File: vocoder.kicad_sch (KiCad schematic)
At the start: 63 parts, among them J1 AudioJack4, J2 Conn_01x02_Socket, J3 Conn_01x02_Pin, J4 USB_C_Receptacle_USB2.0_16P, Q1 Q_NPN_BCE, Q2 Q_NPN_BCE, Q3 AO3401A, Q4 Q_NPN_BCE, SW1 SW_SPDT, SW2 SW_Push, SW3 SW_Push, U1 ESP32-S3-MINI-1, U3 BQ24074RGT, U4 TPS63031DSK, U5 ADAU1761

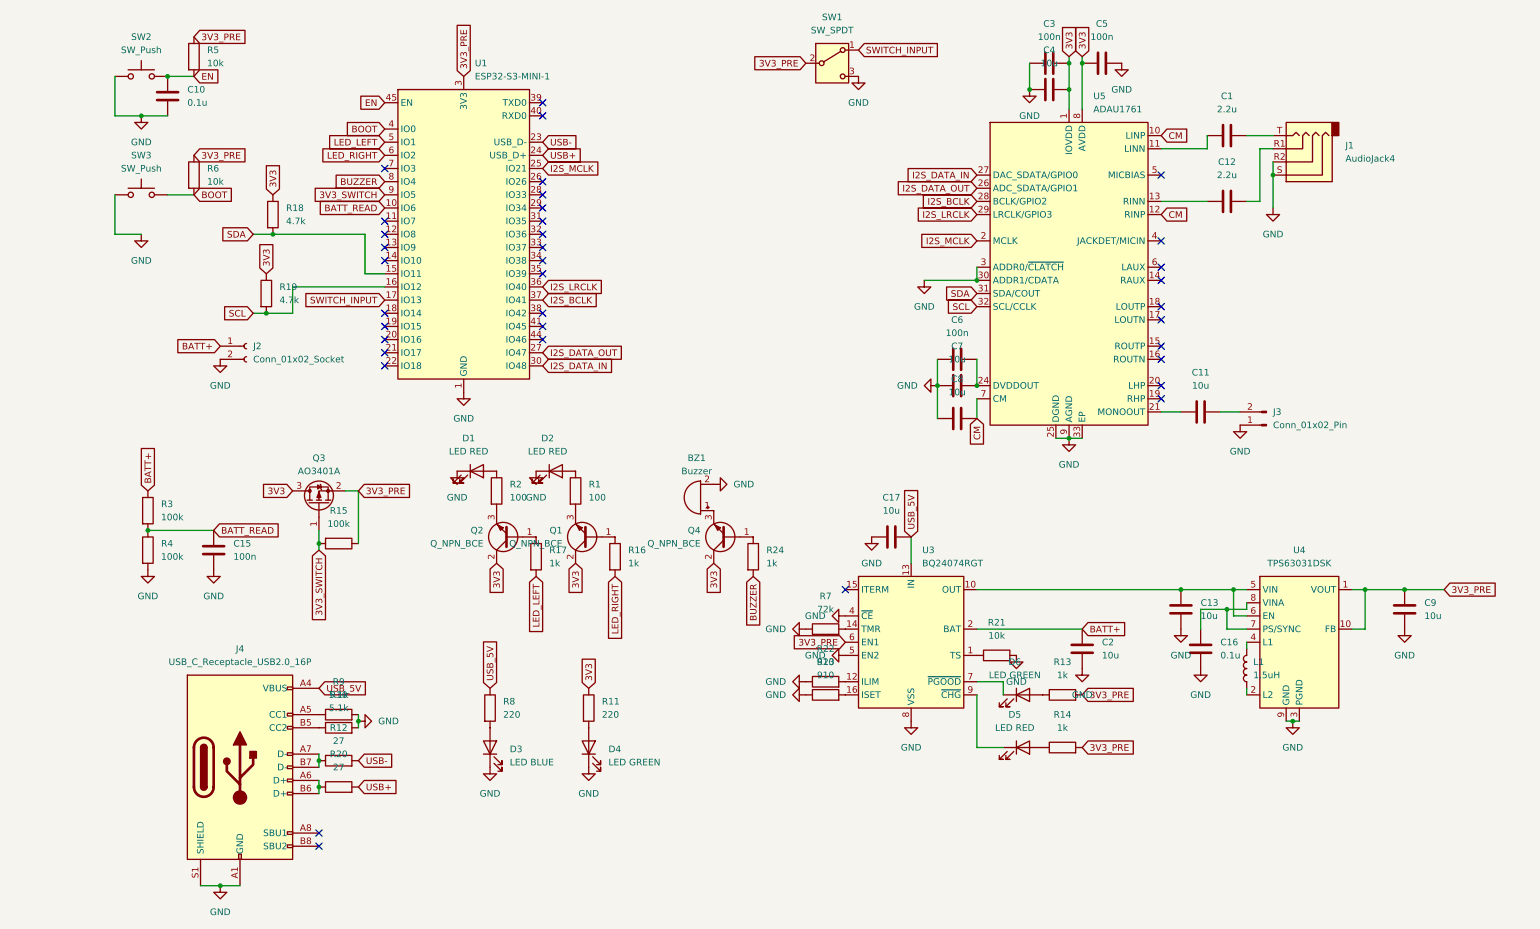
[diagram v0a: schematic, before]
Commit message: replaced esp32-s3 mini with esp32-s3-wroom, added needed op amp and amp
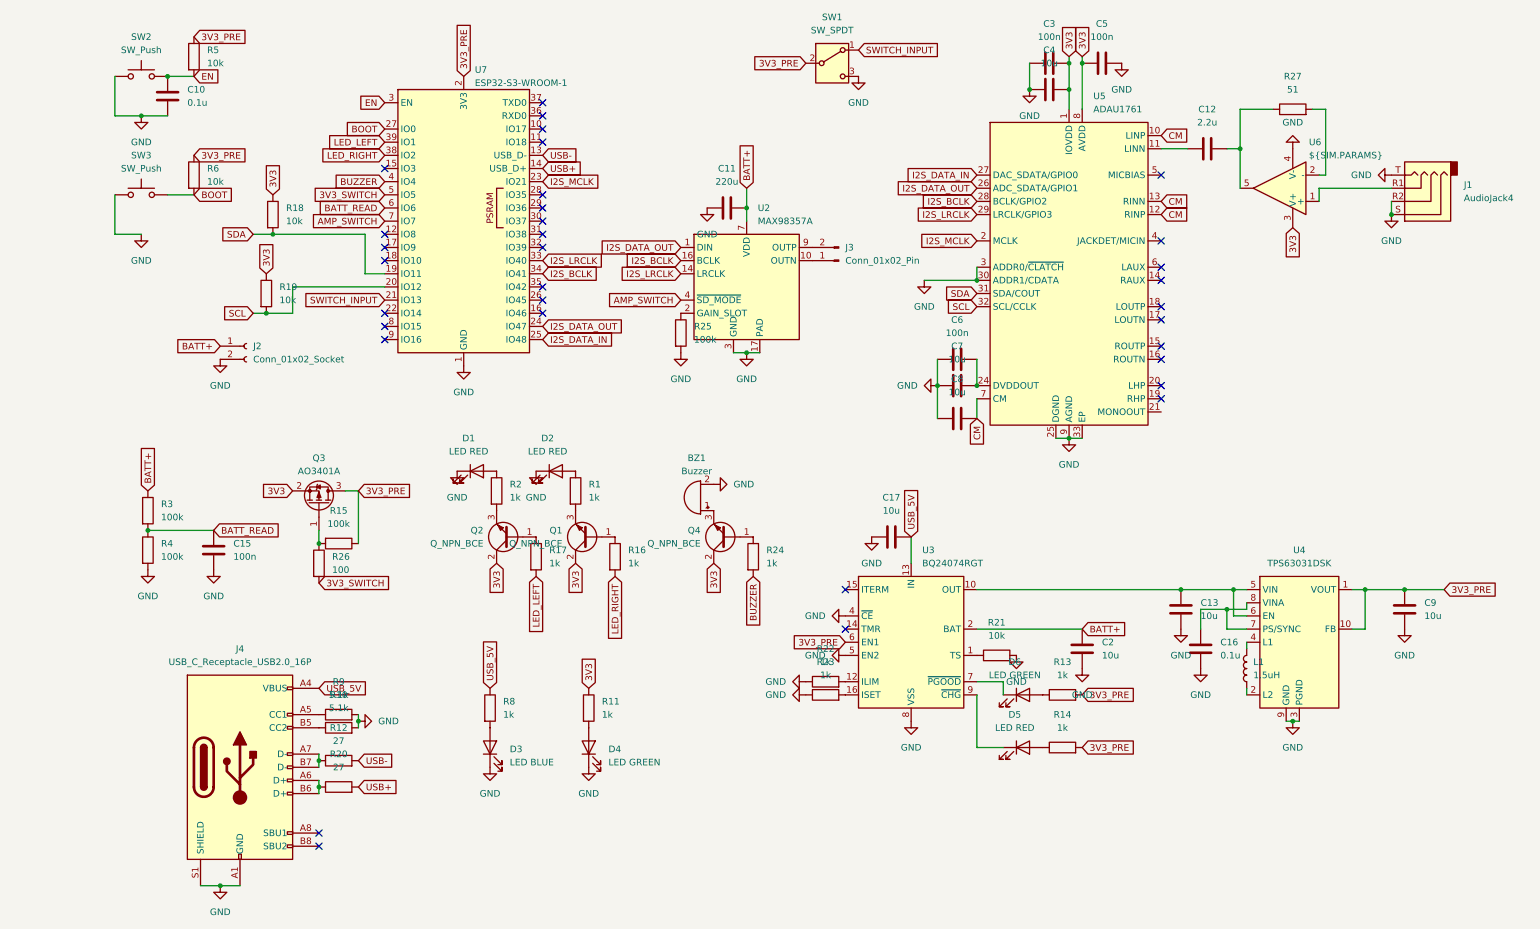
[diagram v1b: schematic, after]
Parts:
- removed C1: 2.2u, Capacitor_SMD:C_0603_1608Metric, symbol Device:C
- removed R7: 72k, Resistor_SMD:R_0603_1608Metric_Pad0.98x0.95mm_HandSolder, symbol Device:R
- removed U1: ESP32-S3-MINI-1, PCM_Espressif:ESP32-S3-MINI-1, symbol RF_Module:ESP32-S3-MINI-1
- added R25: 100k, Resistor_SMD:R_0603_1608Metric_Pad0.98x0.95mm_HandSolder, symbol Device:R
- added R26: 100, Resistor_SMD:R_0603_1608Metric_Pad0.98x0.95mm_HandSolder, symbol Device:R
- added R27: 51, Resistor_SMD:R_0603_1608Metric_Pad0.98x0.95mm_HandSolder, symbol Device:R
- added U2: MAX98357A, Package_DFN_QFN:TQFN-16-1EP_3x3mm_P0.5mm_EP1.23x1.23mm, symbol Audio:MAX98357A
- added U6: ${SIM.PARAMS}, custom_footprints:TLV9041, symbol Simulation_SPICE:OPAMP
- added U7: ESP32-S3-WROOM-1, RF_Module:ESP32-S3-WROOM-1, symbol RF_Module:ESP32-S3-WROOM-1
- C11: value 10u -> 220u
- R1, R2: value 100 -> 1k
- R11, R8: value 220 -> 1k
- R18, R19: value 4.7k -> 10k
- R22, R23: value 910 -> 1k
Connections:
- net 3V3: now also Q3.2 (S), U6.3 (V+); no longer Q3.3 (D)
- net 3V3_PRE: now also Q3.3 (D), U7.2 (3V3); no longer Q3.2 (S)
- net 3V3_SWITCH: now also R26.2, U7.5 (IO5); no longer Q3.1 (G), R15.2
- net BATT+: now also C11.1, U2.7 (VDD), U2.8 (VDD)
- net BATT_READ: now also U7.6 (IO6)
- net BOOT: now also U7.27 (IO0)
- net BUZZER: now also U7.4 (IO4)
- net CM: now also U5.13 (RINN)
- net EN: now also U7.3 (EN)
- net GND: now also C11.2, J1.T, R25.2, U2.11 (GND), U2.15 (GND), U2.17 (PAD), U2.3 (GND), U6.4 (V-), U7.1 (GND), U7.40 (GND), U7.41 (GND); no longer J3.1 (Pin_1)
- net I2S_BCLK: now also U2.16 (BCLK), U7.34 (IO41)
- net I2S_DATA_IN: now also U7.25 (IO48)
- net I2S_DATA_OUT: now also U2.1 (DIN), U7.24 (IO47)
- net I2S_LRCLK: now also U2.14 (LRCLK), U7.33 (IO40)
- net I2S_MCLK: now also U7.23 (IO21)
- net LED_LEFT: now also U7.39 (IO1)
- net LED_RIGHT: now also U7.38 (IO2)
- net SCL: now also U7.20 (IO12)
- net SDA: now also U7.19 (IO11)
- net SWITCH_INPUT: now also U7.21 (IO13)
- net USB+: now also U7.14 (USB_D+)
- net USB-: now also U7.13 (USB_D-)
- net at U5.21 (MONOOUT): no longer C11.1
- net at J3.2 (Pin_2): now also U2.9 (OUTP); no longer C11.2
- net at C12.1: now also U5.11 (LINN); no longer U5.13 (RINN)
- net at C12.2: now also R27.1, U6.5; no longer J1.R1
- new net: Q3.1 (G), R15.2, R26.1
- new net: J3.1 (Pin_1), U2.10 (OUTN)
- new net: R25.1, U2.2 (GAIN_SLOT)
- new net: R27.2, U6.2 (-)
- new net: J1.R1, U6.1 (+)
- new net AMP_SWITCH: U2.4 (~{SD_MODE}), U7.7 (IO7)
- no-connect marks 36 -> 33
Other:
- moved on the sheet: C12, J1, J3, Q3

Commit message: semi working before removing battery and adding necessary changes
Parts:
- removed BZ1: Buzzer, Connector_PinHeader_2.54mm:PinHeader_1x02_P2.54mm_Vertical, symbol Device:Buzzer
- removed C11: 220u, Capacitor_SMD:C_1206_3216Metric, symbol Device:C
- removed C12: 2.2u, Capacitor_SMD:C_0603_1608Metric, symbol Device:C
- removed C13, C17, C9: 10u, Capacitor_SMD:C_0603_1608Metric, symbol Device:C
- removed C15: 100n, Capacitor_SMD:C_0603_1608Metric, symbol Device:C
- removed C16: 0.1u, Capacitor_SMD:C_0603_1608Metric, symbol Device:C
- removed D1, D2, D5: LED RED, LED_SMD:LED_0603_1608Metric, symbol Device:LED
- removed D3: LED BLUE, LED_SMD:LED_0603_1608Metric, symbol Device:LED
- removed D4, D6: LED GREEN, LED_SMD:LED_0603_1608Metric, symbol Device:LED
- removed J1: AudioJack4, Connector_Audio:Jack_3.5mm_PJ320D_Horizontal, symbol Connector_Audio:AudioJack4
- removed J3: Conn_01x02_Pin, TerminalBlock_Phoenix:TerminalBlock_Phoenix_MKDS-1,5-2-5.08_1x02_P5.08mm_Horizontal, symbol Connector:Conn_01x02_Pin
- removed L1: 1.5uH, Inductor_SMD:L_0805_2012Metric, symbol Device:L
- removed Q1, Q2, Q4: Q_NPN_BCE, Package_TO_SOT_SMD:SOT-23, symbol Transistor_BJT:Q_NPN_BCE
- removed R18, R19: 10k, Resistor_SMD:R_0603_1608Metric_Pad0.98x0.95mm_HandSolder, symbol Device:R
- removed R22, R24: 1k, Resistor_SMD:R_0603_1608Metric_Pad0.98x0.95mm_HandSolder, symbol Device:R
- removed R25: 100k, Resistor_SMD:R_0603_1608Metric_Pad0.98x0.95mm_HandSolder, symbol Device:R
- removed R26: 100, Resistor_SMD:R_0603_1608Metric_Pad0.98x0.95mm_HandSolder, symbol Device:R
- removed R27: 51, Resistor_SMD:R_0603_1608Metric_Pad0.98x0.95mm_HandSolder, symbol Device:R
- removed SW1: SW_SPDT, Button_Switch_THT:SW_Slide-03_Wuerth-WS-SLTV_10x2.5x6.4_P2.54mm, symbol Switch:SW_SPDT
- removed U2: MAX98357A, Package_DFN_QFN:TQFN-16-1EP_3x3mm_P0.5mm_EP1.23x1.23mm, symbol Audio:MAX98357A
- removed U3: BQ24074RGT, Package_DFN_QFN:VQFN-16-1EP_3x3mm_P0.5mm_EP1.6x1.6mm, symbol Battery_Management:BQ24074RGT
- removed U4: TPS63031DSK, Package_SON:WSON-10-1EP_2.5x2.5mm_P0.5mm_EP1.2x2mm, symbol Regulator_Switching:TPS63031DSK
- removed U5: ADAU1761, Package_CSP:LFCSP-32-1EP_5x5mm_P0.5mm_EP3.5x3.5mm_ThermalVias, symbol Audio:ADAU1761
- removed U6: ${SIM.PARAMS}, custom_footprints:TLV9041, symbol Simulation_SPICE:OPAMP
- added C1: 1u, Capacitor_SMD:C_0603_1608Metric, symbol Device:C
- added D1, D3, D4: SS34, Diode_SMD:D_SOD-123, symbol Diode:SS34
- added D5, D6: 1N4148, Diode_SMD:D_SOD-323, symbol Diode:1N4148
- added J1: Micro_SD_Card_Det1, MyAntenna_manufacturer:Untitled, symbol Connector:Micro_SD_Card_Det1
- added J5: Conn_02x03_Top_Bottom, Connector_PinHeader_2.54mm:PinHeader_2x03_P2.54mm_Vertical, symbol Connector_Generic:Conn_02x03_Top_Bottom
- added LS1: Speaker, TerminalBlock_Phoenix:TerminalBlock_Phoenix_MKDS-1,5-2-5.08_1x02_P5.08mm_Horizontal, symbol Device:Speaker
- added R7: 10k, Resistor_SMD:R_0603_1608Metric_Pad0.98x0.95mm_HandSolder, symbol Device:R
- added SW1: SW_Push, Button_Switch_SMD:Panasonic_EVQPUJ_EVQPUA, symbol Switch:SW_Push
- added SW4: RotaryEncoder_Switch, Rotary_Encoder:RotaryEncoder_Bourns_Horizontal_PEC12R-2x17F-Sxxxx, symbol Device:RotaryEncoder_Switch
- added U1: MCP73831-2-MC, Package_DFN_QFN:DFN-8-1EP_3x2mm_P0.5mm_EP1.7x1.4mm, symbol Battery_Management:MCP73831-2-MC
- added U2: AP2112K-3.3, Package_TO_SOT_SMD:SOT-23-5, symbol Regulator_Linear:AP2112K-3.3
- added U3: MAX98357A, Package_DFN_QFN:TQFN-16-1EP_3x3mm_P0.5mm_EP1.23x1.23mm, symbol Audio:MAX98357A
- added U4: MAX40200AUK, Package_TO_SOT_SMD:SOT-23-5, symbol Analog_Switch:MAX40200AUK
- C2, C8: value 10u -> 1u
- C3, C6: value 100n -> 1u
- C4, C7: footprint Capacitor_SMD:C_0603_1608Metric -> Capacitor_SMD:C_0805_2012Metric
- C5: value 100n -> 10u; footprint Capacitor_SMD:C_0603_1608Metric -> Capacitor_SMD:C_0805_2012Metric
- R1, R11, R13, R14, R16, R17, R23, R8: value 1k -> 10k
- R2: value 1k -> 2.2k
- R3, R4: value 100k -> 470k
- SW2, SW3: footprint Button_Switch_SMD:SW_Push_SPST_NO_Alps_SKRK -> Button_Switch_SMD:SW_SPST_TS-1088-xR020
- U7: footprint RF_Module:ESP32-S3-WROOM-1 -> RF_Module:ESP32-S3-WROOM-1U
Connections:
- net CM is gone; now on net GND: C8.2
- net SWITCH_INPUT is gone; now on net BUTTON_READ: U7.21 (IO13)
- net 3V3: now also C2.1, C7.2, C8.1, R13.1, R14.1, R16.1, R17.1, R21.1, R23.1, R5.1, R6.1, R8.1, U7.2 (3V3), J1.4 (VDD), J5.1 (Pin_1), R7.1, U2.5 (VOUT); no longer C3.2, C4.2, C5.1, Q3.2 (S)
- net AMP_SWITCH: now also R1.1, U7.31 (IO38), U3.4 (~{SD_MODE}); no longer U7.7 (IO7)
- net BATT+: now also C5.2, U1.3 (V_{BAT}), U1.4 (V_{BAT}), U4.1 (VDD), U4.3 (EN); no longer C2.2
- net BATT_READ: now also U7.10 (IO17); no longer U7.6 (IO6)
- net GND: now also C2.2, C4.2, C5.1, C6.2, R1.2, R2.2, C1.2, J1.6 (VSS), J1.SH (SHIELD), J5.3 (Pin_3), SW1.2, SW4.C, SW4.S2, U1.6 (V_{SS}), U2.2 (GND), U3.11 (GND), U3.15 (GND), U3.17 (PAD), U3.2 (GAIN_SLOT), U3.3 (GND), U4.2 (GND); no longer C2.1, C4.1, C5.2, C6.1, C8.1, R21.2, R23.1
- net I2S_BCLK: now also U7.33 (IO40), J5.4 (Pin_4), U3.16 (BCLK); no longer U7.34 (IO41)
- net I2S_DATA_IN: now also U7.39 (IO1), J5.5 (Pin_5); no longer U7.25 (IO48)
- net I2S_DATA_OUT: now also U7.32 (IO39), U3.1 (DIN); no longer U7.24 (IO47)
- net I2S_LRCLK: now also U7.34 (IO41), J5.6 (Pin_6), U3.14 (LRCLK); no longer U7.33 (IO40)
- net I2S_MCLK: now also U7.38 (IO2), J5.2 (Pin_2); no longer U7.23 (IO21)
- net USB_5V: now also C3.2, C4.1, D1.2 (A), D3.2 (A), U1.1 (V_{DD}), U1.2 (V_{DD}); no longer R8.1
- net at Q3.1 (G): now also R15.1, D5.2 (A), D6.2 (A); no longer R15.2
- net BUTTON_READ: now reaches R23.2
- net BUTTON_READ: now also D6.1 (K), SW1.1
- net D3: now reaches R8.2
- net D3: now also U7.8 (IO15), J1.2 (DAT3/CD)
- net at R2.1: now also U1.8 (PROG)
- net CMD: now reaches R11.2
- net CMD: now also U7.7 (IO7), J1.3 (CMD)
- net POWER_SWITCH: now reaches U7.11 (IO18)
- net POWER_SWITCH: now also D5.1 (K)
- net DET: now reaches U7.22 (IO14)
- net DET: now also J1.9 (DET)
- net D2: now reaches U7.9 (IO16)
- net D2: now also J1.1 (DAT2), R7.2
- removed net 3V3_PRE: Q3.3 (D), R13.2, R14.2, R15.1, R5.1, R6.1, U7.2 (3V3)
- net 3V3_SWITCH renamed D0
- net D0: now also R13.2, J1.7 (DAT0)
- net BUZZER renamed D1
- net D1: now also R14.2, J1.8 (DAT1)
- net LED_LEFT renamed ENC_RIGHT
- net ENC_RIGHT: now also U7.25 (IO48), SW4.B; no longer U7.39 (IO1)
- net LED_RIGHT renamed ENC_LEFT
- net ENC_LEFT: now also U7.23 (IO21), SW4.A; no longer U7.38 (IO2)
- net SCL: no longer names the net of U7.20 (IO12)
- net SDA renamed CHARGE_STATUS
- net CHARGE_STATUS: now also U1.5 (STAT)
- new net: C6.1, D3.1 (K), D4.1 (K), U3.7 (VDD), U3.8 (VDD)
- new net: D1.1 (K), Q3.2 (S), R15.2, U4.5 (OUT)
- new net: LS1.1, U3.9 (OUTP)
- new net: LS1.2, U3.10 (OUTN)
- new net AMP_POWER: C1.1, D4.2 (A), Q3.3 (D), U2.1 (VIN), U2.3 (EN)
- new net CLK: J1.5 (CLK), U7.6 (IO6)
- new net ENC_PUSH: R21.2, SW4.S1, U7.24 (IO47)
- no-connect marks 33 -> 14
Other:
- moved on the sheet: J2, Q3, R15
